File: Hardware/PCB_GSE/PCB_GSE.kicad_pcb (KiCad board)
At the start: 4 copper layers, 74 x 95.6 mm, 155 parts, among them J1 Conn_01x02, J2 BM03B-GHS-TBT, J3 GT17HN-4DP-2H(D)(56), J4 Conn_01x06_Pin, J5 Screw_Terminal_01x04, J6 Screw_Terminal_01x04, J7 Screw_Terminal_01x04, J8 Vin_XT30PW-F, U1 MAX6612MXK, U10 MP28167GQ-B-P, U2 ISOW1044, U3 SI5442DU-T1-GE3, U4 INA125UA/2K5, U5 STM32F103CBT6, U6 SI5442DU-T1-GE3, U7 SI5442DU-T1-GE3, U8 MPQ9843GLE-5-AEC1-Z, U9 TLV75733PDBVR, Y1 830050510

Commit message: wip(moteur + gse): fix silkscreen + traces + polygons
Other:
- board text added: "5V-7.4V"
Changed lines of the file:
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@@
+		)
+	)
+	(gr_text "5V-7.4V"
+		(at 116.5352 130.8608 270)
+		(layer "B.SilkS")
+		(effects
+			(font
+				(size 1 1)
+				(thickness 0.2)
+				(bold yes)
+			)
+			(justify bottom mirror)
 		)
 	)

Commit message: Fix : servo side connectors
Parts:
- added REF**: MountingHole_2.1mm, MountingHole:MountingHole_2.1mm, F.Cu at (185.5, 84.2)
- added REF**: MountingHole_2.1mm, MountingHole:MountingHole_2.1mm, F.Cu at (118.7, 102.5)
- added REF**: MountingHole_2.1mm, MountingHole:MountingHole_2.1mm, F.Cu at (118.7, 98.4)
- J2: footprint pcb_moteur:CONN_BM03B-GHS-TBT_JST -> pcb_moteur:JST_SM03B-GHS-TB
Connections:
- J2 pad 4: (no net) -> unconnected-(J2-Case-Pad4)_1

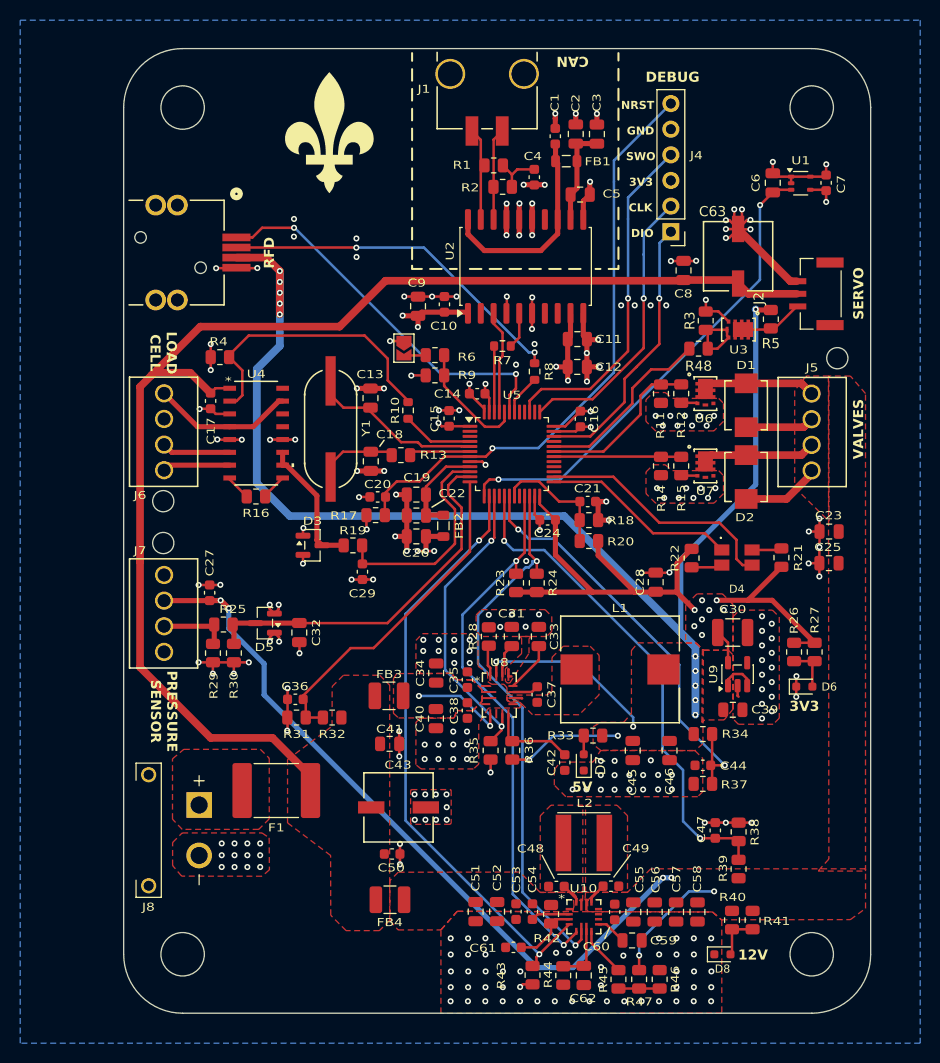
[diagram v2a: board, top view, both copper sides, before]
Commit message: fix : BOM errors, change cutoff freq for moteur, minor fixes for GSE
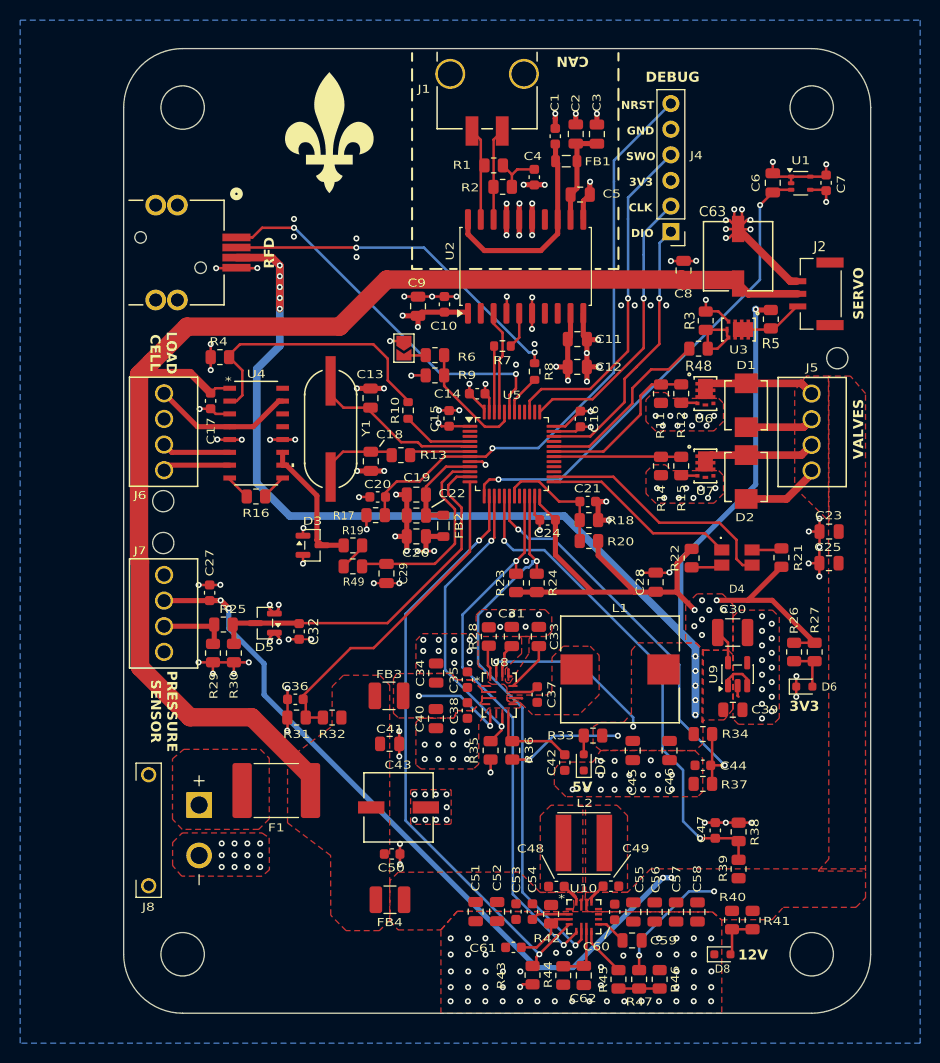
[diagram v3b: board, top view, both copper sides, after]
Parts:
- added R49: 1.5k, Resistor_SMD:R_0805_2012Metric, F.Cu at (137.5, 104.9)
- C29: value 100nF -> 1uF; footprint Capacitor_SMD:C_0603_1608Metric -> Capacitor_SMD:C_0805_2012Metric
- C32: value 10nF -> 100nF; footprint Capacitor_SMD:C_0805_2012Metric -> Capacitor_SMD:C_0603_1608Metric
- F1: value 2920L700/24SLER -> 10A trip 5A hold
- moved C29 2.39 mm to (140.8, 105.6)
- moved C32 0.11 mm to (132.1, 111.3)
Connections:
- R19 pad 2: LCell_An -> Net-(R19-Pad2)
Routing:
- net Net-(R19-Pad2): track 0.00 -> 2.88 mm
- net VIN_Filtered: track 129.5 -> 131.7 mm
- net LCell_An: track 21.7 -> 19.8 mm
- net GND: track 146.0 -> 147.8 mm, vias 232 -> 233
- net LCell_Sleep: track 28.6 -> 27.9 mm

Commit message: fix(gse): Vin trace
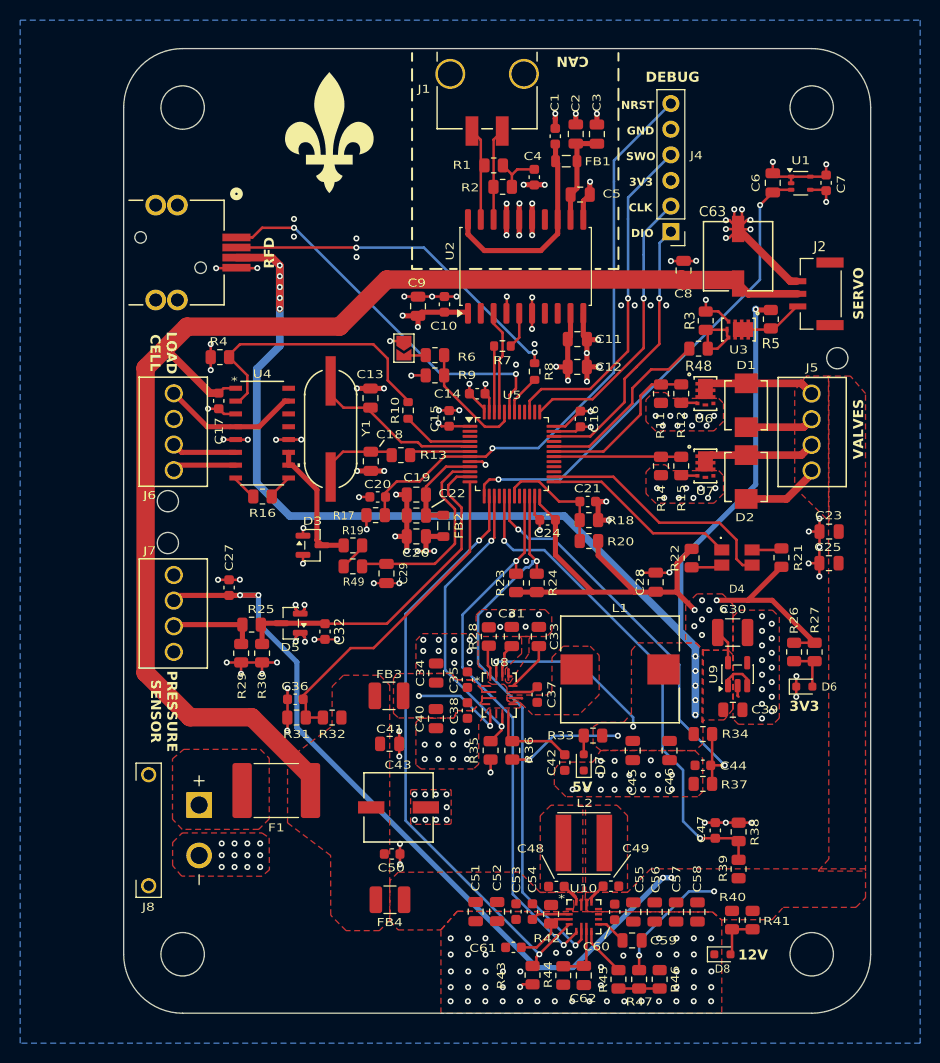
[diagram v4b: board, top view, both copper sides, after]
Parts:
- moved R29 2.79 mm to (126.4, 113.5)
- moved R30 2.79 mm to (128.5, 113.5)
- moved R25 2.79 mm to (127.4, 110.6)
- moved C32 2.56 mm to (134.7, 111.3)
- moved D5 2.56 mm to (131.3, 110.5)
- moved C27 1.99 mm to (125.2, 107.0)
- moved J6 0.96 mm to (119.7, 87.7)
- moved J7 0.96 mm to (119.7, 105.7)
- moved C17 0.81 mm to (124.2, 88.5)
- moved R16 0.65 mm to (128.5, 97.9)
- moved U4 0.59 mm to (128.5, 91.7)
- moved REF** 0.46 mm to (119.1, 102.5)
- moved REF** 0.46 mm to (119.1, 98.4)
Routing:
- net Pressure_An: track 37.1 -> 34.4 mm
- net Vin_Valve: track 100.2 -> 102.8 mm
- net Net-(J7-Pin_3): track 7.39 -> 9.08 mm
- net VIN_Filtered: track 131.7 -> 130.1 mm
- net LC_IN+: track 14.2 -> 13.2 mm
